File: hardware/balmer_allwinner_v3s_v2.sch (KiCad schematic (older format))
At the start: 32 parts, among them U1 AllwinnerV3S

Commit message: Some routing done
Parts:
- added C38, C39: 100n, Capacitor_SMD:C_0603_1608Metric, symbol Device:C
- added R24, R25: 33R, Resistor_SMD:R_0603_1608Metric, symbol Device:R
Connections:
- net labels added: USB_D-D+, USB_D-D-, WAKE
- net labels removed: PB4
- wire segments 110 -> 116
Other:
- moved on the sheet: C1, C10, C11, C12, C13, C14, C15, C16, C17, C18, C19, C2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

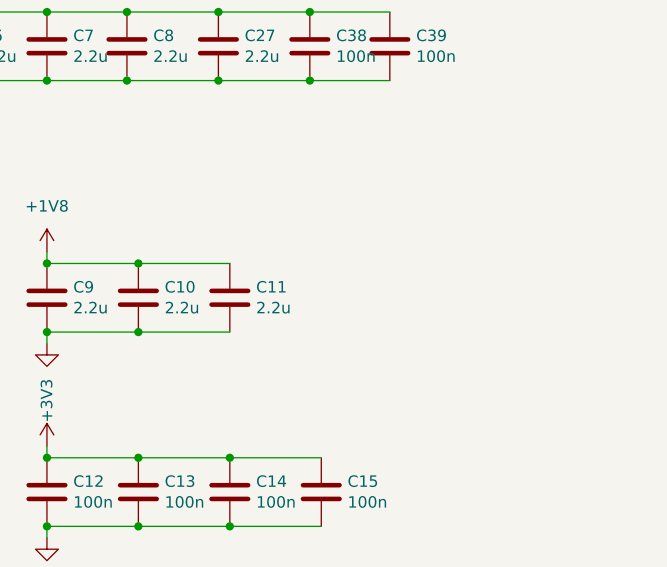
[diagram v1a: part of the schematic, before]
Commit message: More routing. CPU power routed. USB li-ion charging added
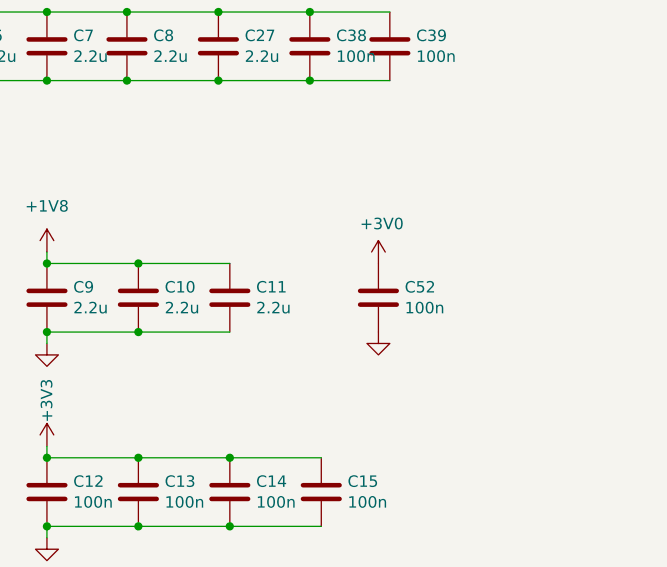
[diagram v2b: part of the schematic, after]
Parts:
- added C52: 100n, Capacitor_SMD:C_0603_1608Metric, symbol Device:C
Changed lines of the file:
@@
 Text Label 4700 1650 1    50   ~ 0
 USB_D-D-
+$Comp
+L Device:C C52
+U 1 1 624A12C5
+P 9900 2800
+F 0 "C52" H 10015 2846 50  0000 L CNN
+F 1 "100n" H 10015 2755 50  0000 L CNN
+F 2 "Capacitor_SMD:C_0603_1608Metric" H 9938 2650 50  0001 C CNN
+F 3 "~" H 9900 2800 50  0001 C CNN
+	1    9900 2800
+	1    0    0    -1
+$EndComp
+$Comp
+L power:+3V0 #PWR06
+U 1 1 624A1DD9
+P 9900 2650
+F 0 "#PWR06" H 9900 2500 50  0001 C CNN
+F 1 "+3V0" H 9915 2823 50  0000 C CNN
+F 2 "" H 9900 2650 50  0001 C CNN
+F 3 "" H 9900 2650 50  0001 C CNN
+	1    9900 2650
+	1    0    0    -1
+$EndComp
+$Comp
+L power:GND #PWR08
+U 1 1 624A2947
+P 9900 2950
+F 0 "#PWR08" H 9900 2700 50  0001 C CNN
+F 1 "GND" H 9905 2777 50  0001 C CNN
+F 2 "" H 9900 2950 50  0001 C CNN
+F 3 "" H 9900 2950 50  0001 C CNN
+	1    9900 2950
+	1    0    0    -1
+$EndComp
 $EndSCHEMATC

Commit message: backup
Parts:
- added C48: 100n, Capacitor_SMD:C_0603_1608Metric, symbol Device:C
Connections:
- wire segments 116 -> 118
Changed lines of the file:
@@
 	1    0    0    -1
 $EndComp
+$Comp
+L Device:C C48
+U 1 1 62625E68
+P 10300 2800
+F 0 "C48" H 10415 2846 50  0000 L CNN
+F 1 "100n" H 10415 2755 50  0000 L CNN
+F 2 "Capacitor_SMD:C_0603_1608Metric" H 10338 2650 50  0001 C CNN
+F 3 "~" H 10300 2800 50  0001 C CNN
+	1    10300 2800
+	1    0    0    -1
+$EndComp
+Wire Wire Line
+	9900 2650 10300 2650
+Connection ~ 9900 2650
+Wire Wire Line
+	10300 2950 9900 2950
+Connection ~ 9900 2950
 $EndSCHEMATC

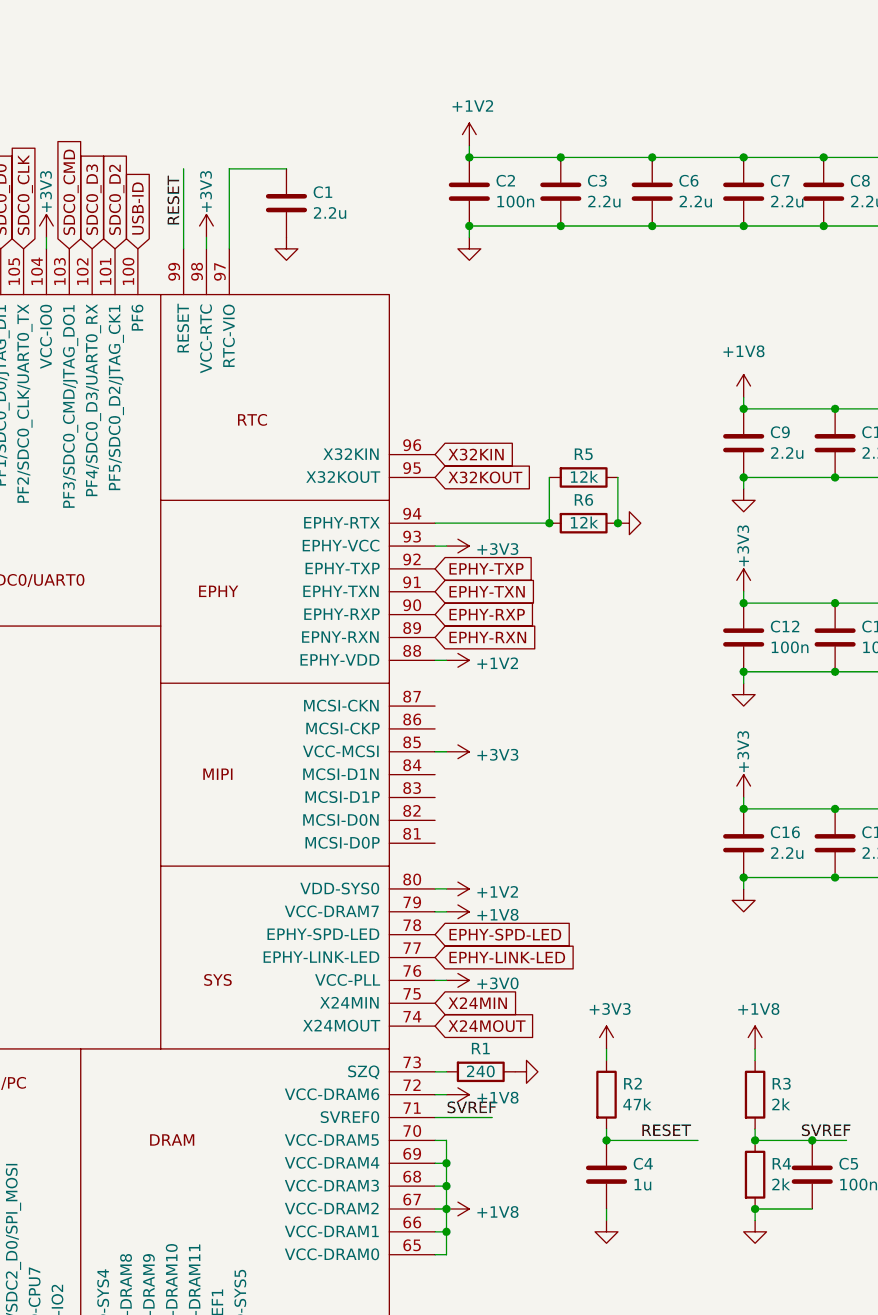
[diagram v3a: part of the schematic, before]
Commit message: Added USB UART
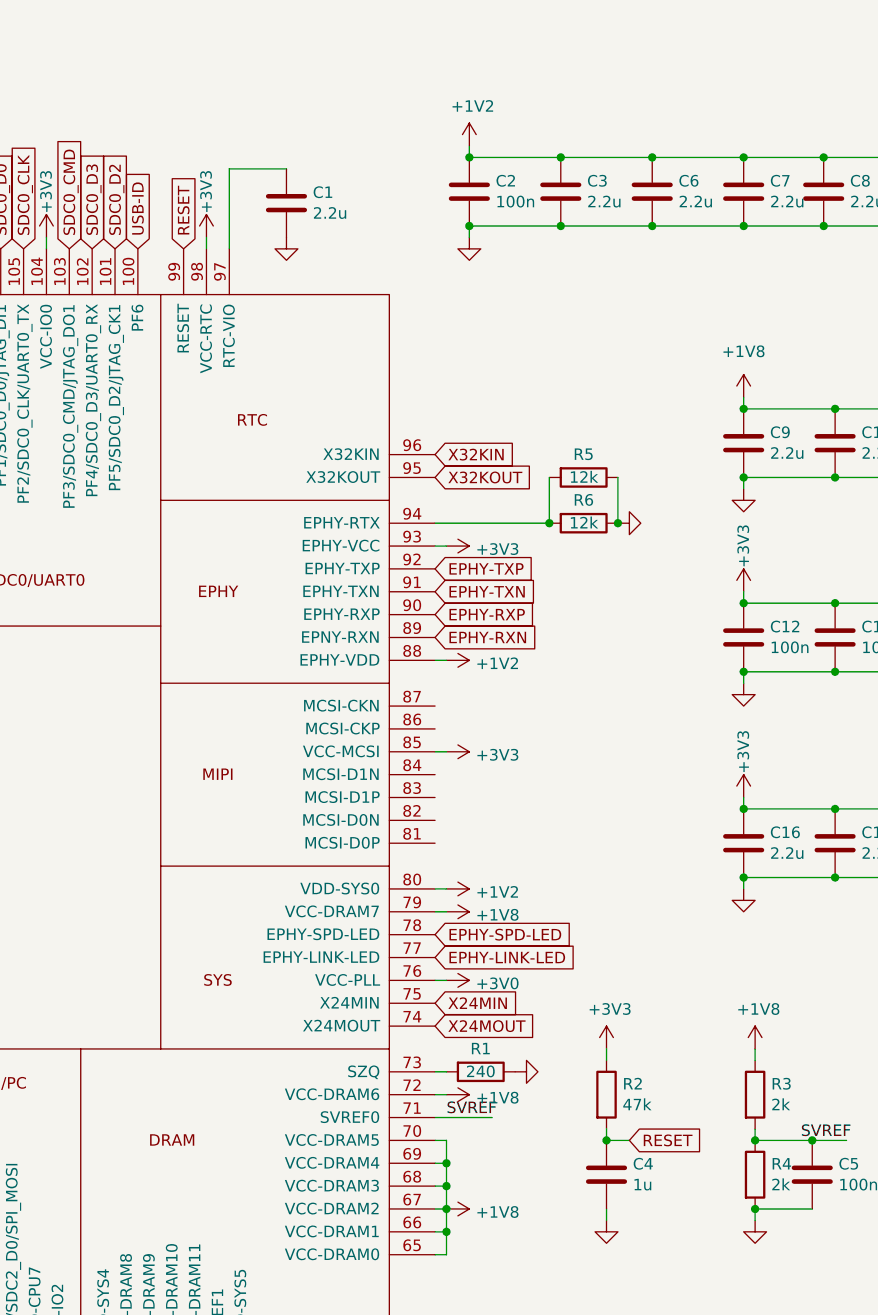
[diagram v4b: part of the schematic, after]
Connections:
- wire segments 118 -> 117
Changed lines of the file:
@@
 Wire Wire Line
 	7850 6150 7850 6200
-Wire Wire Line
-	7850 5850 8250 5850
-Connection ~ 7850 5850
-Text Label 8000 5850 0    50   ~ 0
-RESET
-Wire Wire Line
-	6000 1600 6000 1950
-Text Label 6000 1850 1    50   ~ 0
-RESET
 $Sheet
 S 850  7250 550  200
@@
 	10300 2950 9900 2950
 Connection ~ 9900 2950
+Text GLabel 6000 1950 1    50   Input ~ 0
+RESET
+Text GLabel 7950 5850 2    50   Input ~ 0
+RESET
+Wire Wire Line
+	7950 5850 7850 5850
+Connection ~ 7850 5850
 $EndSCHEMATC
